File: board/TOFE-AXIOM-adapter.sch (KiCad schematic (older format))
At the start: 21 parts, among them CN1 C, U1 24AA01/24LC01B

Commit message: Adding annotations and parts.
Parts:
- CI2CN1, CI2CS1: footprint (none) -> Pin_Headers:Pin_Header_Straight_1x04
- CV1, CV2, CV3: footprint (none) -> SMD_Packages:SMD-1206_Pol
- CV4, CV5, CV6: footprint (none) -> Capacitors_SMD:C_1206_HandSoldering
- U2, U3: renamed from U?; footprint TO-220 -> Power_Integrations:TO-220
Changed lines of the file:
@@
 	5600 2850 5700 2850
 Wire Wire Line
-	5700 8300 5700 2850
+	5700 2850 5700 8300
 Wire Wire Line
 	5700 4150 5600 4150
@@
 Connection ~ 5700 7450
 Wire Wire Line
-	3800 8300 5700 8300
+	5700 8300 3800 8300
 Connection ~ 3800 7750
 Connection ~ 5700 7750
@@
 	10740 2390 10780 2390
 Wire Wire Line
-	10780 4720 10780 2390
+	10780 2390 10780 4720
 Wire Wire Line
 	10740 2690 10780 2690
@@
 Connection ~ 10780 3690
 Wire Wire Line
-	9010 4720 10780 4720
+	10780 4720 9010 4720
 Connection ~ 10780 4290
 Wire Wire Line
 	9040 4290 9010 4290
 Wire Wire Line
-	9010 3990 9010 4720
+	9010 4720 9010 3990
 Wire Wire Line
 	9010 3990 9040 3990
 Connection ~ 9010 4290
 $Comp
-L GND #PWR3
+L GND #PWR5
 U 1 1 56EBC288
 P 9940 4780
-F 0 "#PWR3" H 9940 4530 50  0001 C CNN
+F 0 "#PWR5" H 9940 4530 50  0001 C CNN
 F 1 "GND" H 9940 4630 50  0000 C CNN
 F 2 "" H 9940 4780 50  0000 C CNN
@@
 Connection ~ 10980 3390
 $Comp
-L GND #PWR5
+L GND #PWR7
 U 1 1 56EBCC2F
 P 11440 3500
-F 0 "#PWR5" H 11440 3250 50  0001 C CNN
+F 0 "#PWR7" H 11440 3250 50  0001 C CNN
 F 1 "GND" H 11440 3350 50  0000 C CNN
 F 2 "" H 11440 3500 50  0000 C CNN
@@
 	10740 5510 10780 5510
 Wire Wire Line
-	10780 7840 10780 5510
+	10780 5510 10780 7840
 Wire Wire Line
 	10740 5810 10780 5810
@@
 Connection ~ 10780 6810
 Wire Wire Line
-	9010 7840 10780 7840
+	10780 7840 9010 7840
 Connection ~ 10780 7410
 Wire Wire Line
 	9040 7410 9010 7410
 Wire Wire Line
-	9010 7110 9010 7840
+	9010 7840 9010 7110
 Wire Wire Line
 	9010 7110 9040 7110
 Connection ~ 9010 7410
 $Comp
-L GND #PWR4
+L GND #PWR6
 U 1 1 56EBD984
 P 9940 7900
-F 0 "#PWR4" H 9940 7650 50  0001 C CNN
+F 0 "#PWR6" H 9940 7650 50  0001 C CNN
 F 1 "GND" H 9940 7750 50  0000 C CNN
 F 2 "" H 9940 7900 50  0000 C CNN
@@
 Connection ~ 10980 6510
 $Comp
-L GND #PWR6
+L GND #PWR8
 U 1 1 56EBD9A0
 P 11440 6620
-F 0 "#PWR6" H 11440 6370 50  0001 C CNN
+F 0 "#PWR8" H 11440 6370 50  0001 C CNN
 F 1 "GND" H 11440 6470 50  0000 C CNN
 F 2 "" H 11440 6620 50  0000 C CNN
@@
 F 0 "CI2CS1" H 8290 5810 50  0000 C CNN
 F 1 "CONN_01X04" V 8390 5560 50  0000 C CNN
-F 2 "" H 8290 5560 50  0000 C CNN
+F 2 "Pin_Headers:Pin_Header_Straight_1x04" H 8290 5560 50  0001 C CNN
 F 3 "" H 8290 5560 50  0000 C CNN
 	1    8290 5560
@@
 F 0 "CI2CN1" H 8290 2690 50  0000 C CNN
 F 1 "CONN_01X04" V 8390 2440 50  0000 C CNN
-F 2 "" H 8290 2440 50  0000 C CNN
+F 2 "Pin_Headers:Pin_Header_Straight_1x04" H 8290 2440 50  0001 C CNN
 F 3 "" H 8290 2440 50  0000 C CNN
 	1    8290 2440
@@
 $EndComp
 $Comp
-L GND #PWR?
+L GND #PWR3
 U 1 1 56EF4A15
 P 8760 2290
-F 0 "#PWR?" H 8760 2040 50  0001 C CNN
+F 0 "#PWR3" H 8760 2040 50  0001 C CNN
 F 1 "GND" H 8760 2140 50  0000 C CNN
 F 2 "" H 8760 2290 50  0000 C CNN
@@
 	8760 2290 8490 2290
 $Comp
-L GND #PWR?
+L GND #PWR4
 U 1 1 56EF4B73
 P 8760 5410
-F 0 "#PWR?" H 8760 5160 50  0001 C CNN
+F 0 "#PWR4" H 8760 5160 50  0001 C CNN
 F 1 "GND" H 8760 5260 50  0000 C CNN
 F 2 "" H 8760 5410 50  0000 C CNN
@@
 	12170 1540 15770 1540
 $Comp
-L LM317T U?
+L LM317T U2
 U 1 1 56F236A7
 P 13010 2450
-F 0 "U?" H 12810 2650 50  0000 C CNN
+F 0 "U2" H 12810 2650 50  0000 C CNN
 F 1 "LM317T" H 13010 2650 50  0000 L CNN
-F 2 "TO-220" H 13010 2550 50  0000 C CIN
+F 2 "Power_Integrations:TO-220" H 13010 2550 50  0000 C CIN
 F 3 "" H 13010 2450 50  0000 C CNN
 	1    13010 2450
@@
 $EndComp
 $Comp
-L LM7805CT U?
+L LM7805CT U3
 U 1 1 56F237BB
 P 15010 2450
-F 0 "U?" H 14810 2650 50  0000 C CNN
+F 0 "U3" H 14810 2650 50  0000 C CNN
 F 1 "LM7805CT" H 15010 2650 50  0000 L CNN
-F 2 "TO-220" H 15010 2550 50  0000 C CIN
+F 2 "Power_Integrations:TO-220" H 15010 2550 50  0000 C CIN
 F 3 "" H 15010 2450 50  0000 C CNN
 	1    15010 2450
@@
 	12170 1740 15770 1740
 $Comp
-L GND #PWR?
+L GND #PWR11
 U 1 1 56F23FEE
 P 15010 2740
-F 0 "#PWR?" H 15010 2490 50  0001 C CNN
+F 0 "#PWR11" H 15010 2490 50  0001 C CNN
 F 1 "GND" H 15010 2590 50  0000 C CNN
 F 2 "" H 15010 2740 50  0000 C CNN
@@
 $EndComp
 $Comp
-L GND #PWR?
+L GND #PWR9
 U 1 1 56F2402D
 P 13010 2740
-F 0 "#PWR?" H 13010 2490 50  0001 C CNN
+F 0 "#PWR9" H 13010 2490 50  0001 C CNN
 F 1 "GND" H 13010 2590 50  0000 C CNN
 F 2 "" H 13010 2740 50  0000 C CNN
@@
 	14110 3200 14560 3200
 $Comp
-L GND #PWR?
+L GND #PWR10
 U 1 1 56F25B7E
 P 13710 3630
-F 0 "#PWR?" H 13710 3380 50  0001 C CNN
+F 0 "#PWR10" H 13710 3380 50  0001 C CNN
 F 1 "GND" H 13710 3480 50  0000 C CNN
 F 2 "" H 13710 3630 50  0000 C CNN
@@
 F 0 "CV3" H 13485 3460 50  0000 L CNN
 F 1 "CP1" H 13485 3260 50  0000 L CNN
-F 2 "" H 13460 3360 50  0000 C CNN
+F 2 "SMD_Packages:SMD-1206_Pol" H 13460 3360 50  0001 C CNN
 F 3 "" H 13460 3360 50  0000 C CNN
 	1    13460 3360
@@
 F 0 "CV4" H 14135 3470 50  0000 L CNN
 F 1 "C" H 14135 3270 50  0000 L CNN
-F 2 "" H 14148 3220 50  0000 C CNN
+F 2 "Capacitors_SMD:C_1206_HandSoldering" H 14148 3220 50  0001 C CNN
 F 3 "" H 14110 3370 50  0000 C CNN
 	1    14110 3370
@@
 F 0 "CV5" H 14365 3470 50  0000 L CNN
 F 1 "C" H 14365 3270 50  0000 L CNN
-F 2 "" H 14378 3220 50  0000 C CNN
+F 2 "Capacitors_SMD:C_1206_HandSoldering" H 14378 3220 50  0001 C CNN
 F 3 "" H 14340 3370 50  0000 C CNN
 	1    14340 3370
@@
 F 0 "CV6" H 14585 3470 50  0000 L CNN
 F 1 "C" H 14585 3270 50  0000 L CNN
-F 2 "" H 14598 3220 50  0000 C CNN
+F 2 "Capacitors_SMD:C_1206_HandSoldering" H 14598 3220 50  0001 C CNN
 F 3 "" H 14560 3370 50  0000 C CNN
 	1    14560 3370
@@
 F 0 "CV2" H 13255 3460 50  0000 L CNN
 F 1 "CP1" H 13255 3260 50  0000 L CNN
-F 2 "" H 13230 3360 50  0000 C CNN
+F 2 "SMD_Packages:SMD-1206_Pol" H 13230 3360 50  0001 C CNN
 F 3 "" H 13230 3360 50  0000 C CNN
 	1    13230 3360
@@
 F 0 "CV1" H 13025 3460 50  0000 L CNN
 F 1 "CP1" H 13025 3260 50  0000 L CNN
-F 2 "" H 13000 3360 50  0000 C CNN
+F 2 "SMD_Packages:SMD-1206_Pol" H 13000 3360 50  0001 C CNN
 F 3 "" H 13000 3360 50  0000 C CNN
 	1    13000 3360

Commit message: Updates from Dejan Stevanovic.
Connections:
- net labels removed: SCL, SDA
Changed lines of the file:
@@
 LIBS:valves
 LIBS:TOFE-AXIOM-adapter-cache
-LIBS:TOFE
-LIBS:axiom
-LIBS:EEPROM
 EELAYER 25 0
 EELAYER END
@@
 Connection ~ 9010 4290
 $Comp
-L GND #PWR5
+L GND #PWR01
 U 1 1 56EBC288
 P 9940 4780
-F 0 "#PWR5" H 9940 4530 50  0001 C CNN
+F 0 "#PWR01" H 9940 4530 50  0001 C CNN
 F 1 "GND" H 9940 4630 50  0000 C CNN
 F 2 "" H 9940 4780 50  0000 C CNN
@@
 Connection ~ 10980 3390
 $Comp
-L GND #PWR7
+L GND #PWR02
 U 1 1 56EBCC2F
 P 11440 3500
-F 0 "#PWR7" H 11440 3250 50  0001 C CNN
+F 0 "#PWR02" H 11440 3250 50  0001 C CNN
 F 1 "GND" H 11440 3350 50  0000 C CNN
 F 2 "" H 11440 3500 50  0000 C CNN
@@
 	11440 3500 11340 3500
 $Comp
-L GND #PWR1
+L GND #PWR03
 U 1 1 56EBCF33
 P 4700 8350
-F 0 "#PWR1" H 4700 8100 50  0001 C CNN
+F 0 "#PWR03" H 4700 8100 50  0001 C CNN
 F 1 "GND" H 4700 8200 50  0000 C CNN
 F 2 "" H 4700 8350 50  0000 C CNN
@@
 GND
 Text Label 4200 9300 0    60   ~ 12
-SCL
+S_SCL
 Text Label 4200 9700 0    60   ~ 12
-SDA
+S_SDA
 Text Notes 5050 9000 0    60   ~ 12
 EEPROM
@@
 	6000 10050 6000 10100
 $Comp
-L GND #PWR2
+L GND #PWR04
 U 1 1 56EBC6DB
 P 6000 9350
-F 0 "#PWR2" H 6000 9100 50  0001 C CNN
+F 0 "#PWR04" H 6000 9100 50  0001 C CNN
 F 1 "GND" H 6000 9200 50  0000 C CNN
 F 2 "" H 6000 9350 50  0000 C CNN
@@
 Connection ~ 9010 7410
 $Comp
-L GND #PWR6
+L GND #PWR05
 U 1 1 56EBD984
 P 9940 7900
-F 0 "#PWR6" H 9940 7650 50  0001 C CNN
+F 0 "#PWR05" H 9940 7650 50  0001 C CNN
 F 1 "GND" H 9940 7750 50  0000 C CNN
 F 2 "" H 9940 7900 50  0000 C CNN
@@
 Connection ~ 10980 6510
 $Comp
-L GND #PWR8
+L GND #PWR06
 U 1 1 56EBD9A0
 P 11440 6620
-F 0 "#PWR8" H 11440 6370 50  0001 C CNN
+F 0 "#PWR06" H 11440 6370 50  0001 C CNN
 F 1 "GND" H 11440 6470 50  0000 C CNN
 F 2 "" H 11440 6620 50  0000 C CNN
@@
 $EndComp
 $Comp
-L GND #PWR3
+L GND #PWR07
 U 1 1 56EF4A15
 P 8760 2290
-F 0 "#PWR3" H 8760 2040 50  0001 C CNN
+F 0 "#PWR07" H 8760 2040 50  0001 C CNN
 F 1 "GND" H 8760 2140 50  0000 C CNN
 F 2 "" H 8760 2290 50  0000 C CNN
@@
 	8760 2290 8490 2290
 $Comp
-L GND #PWR4
+L GND #PWR08
 U 1 1 56EF4B73
 P 8760 5410
-F 0 "#PWR4" H 8760 5160 50  0001 C CNN
+F 0 "#PWR08" H 8760 5160 50  0001 C CNN
 F 1 "GND" H 8760 5260 50  0000 C CNN
 F 2 "" H 8760 5410 50  0000 C CNN
@@
 	12170 1740 15770 1740
 $Comp
-L GND #PWR11
+L GND #PWR09
 U 1 1 56F23FEE
 P 15010 2740
-F 0 "#PWR11" H 15010 2490 50  0001 C CNN
+F 0 "#PWR09" H 15010 2490 50  0001 C CNN
 F 1 "GND" H 15010 2590 50  0000 C CNN
 F 2 "" H 15010 2740 50  0000 C CNN
@@
 $EndComp
 $Comp
-L GND #PWR9
+L GND #PWR010
 U 1 1 56F2402D
 P 13010 2740
-F 0 "#PWR9" H 13010 2490 50  0001 C CNN
+F 0 "#PWR010" H 13010 2490 50  0001 C CNN
 F 1 "GND" H 13010 2590 50  0000 C CNN
 F 2 "" H 13010 2740 50  0000 C CNN
@@
 	14110 3200 14560 3200
 $Comp
-L GND #PWR10
+L GND #PWR011
 U 1 1 56F25B7E
 P 13710 3630
-F 0 "#PWR10" H 13710 3380 50  0001 C CNN
+F 0 "#PWR011" H 13710 3380 50  0001 C CNN
 F 1 "GND" H 13710 3480 50  0000 C CNN
 F 2 "" H 13710 3630 50  0000 C CNN

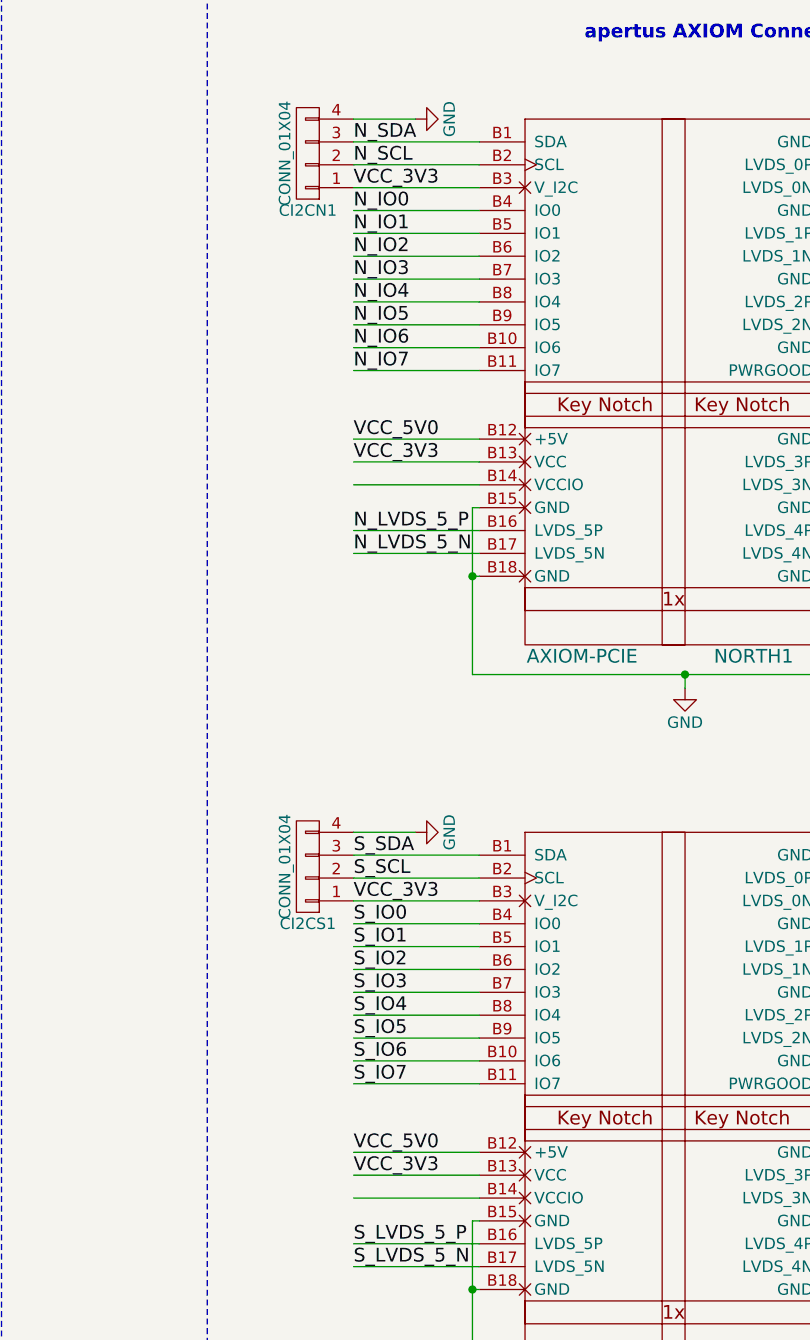
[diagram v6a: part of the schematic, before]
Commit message: Make VCC names consistent.
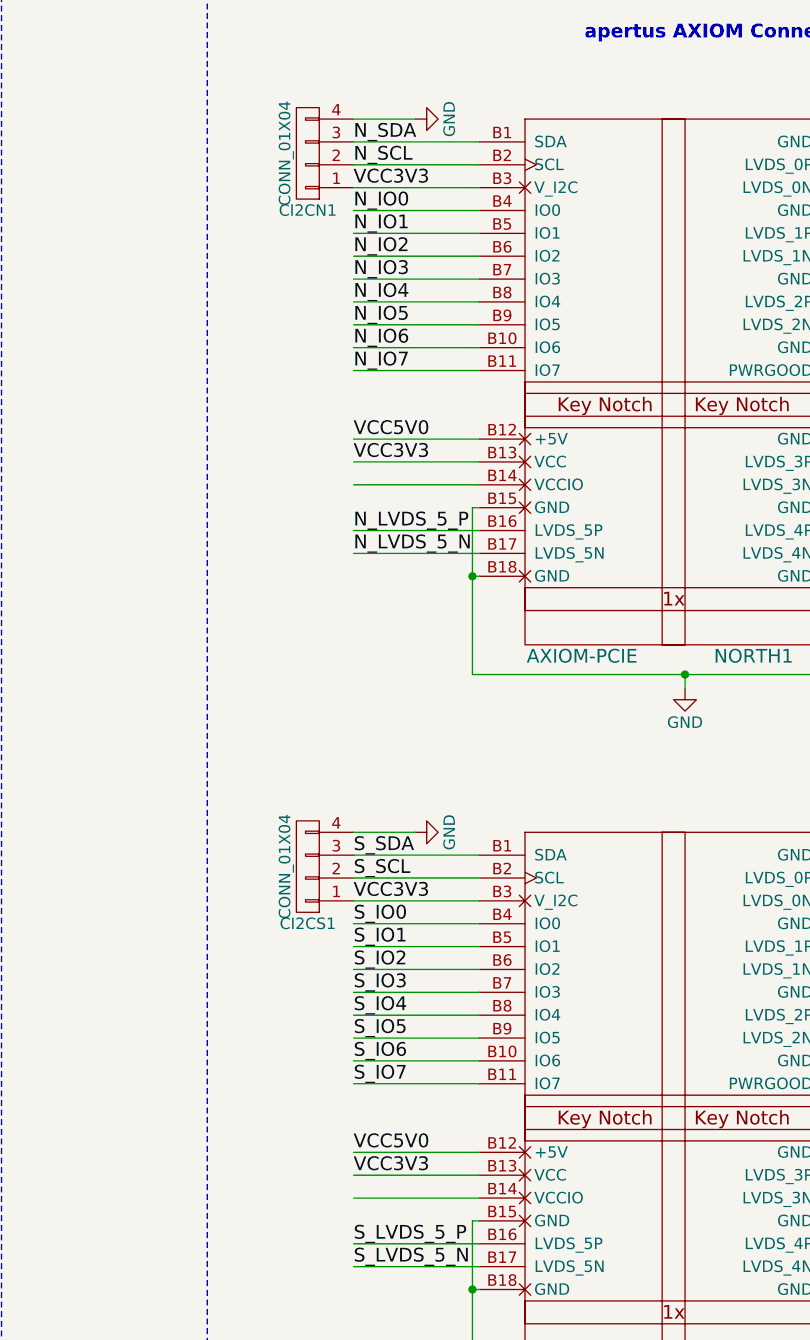
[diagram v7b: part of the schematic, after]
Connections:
- net labels added: VCC5V0
- net labels removed: VCC_3V3, VCC_5V0
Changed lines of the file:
@@
 	8490 3690 9040 3690
 Text Label 8490 3690 0    60   ~ 0
-VCC_5V0
+VCC5V0
 Text Label 8490 2590 0    60   ~ 0
-VCC_3V3
+VCC3V3
 Wire Wire Line
 	10740 3390 10980 3390
@@
 	8490 6810 9040 6810
 Text Label 8490 6810 0    60   ~ 0
-VCC_5V0
+VCC5V0
 Text Label 8490 5710 0    60   ~ 0
-VCC_3V3
+VCC3V3
 Wire Wire Line
 	10740 6510 10980 6510
@@
 	11440 6620 11340 6620
 Text Label 8490 3790 0    60   ~ 0
-VCC_3V3
+VCC3V3
 Text Label 8490 6910 0    60   ~ 0
-VCC_3V3
+VCC3V3
 $Comp
 L CONN_01X04 CI2CS1

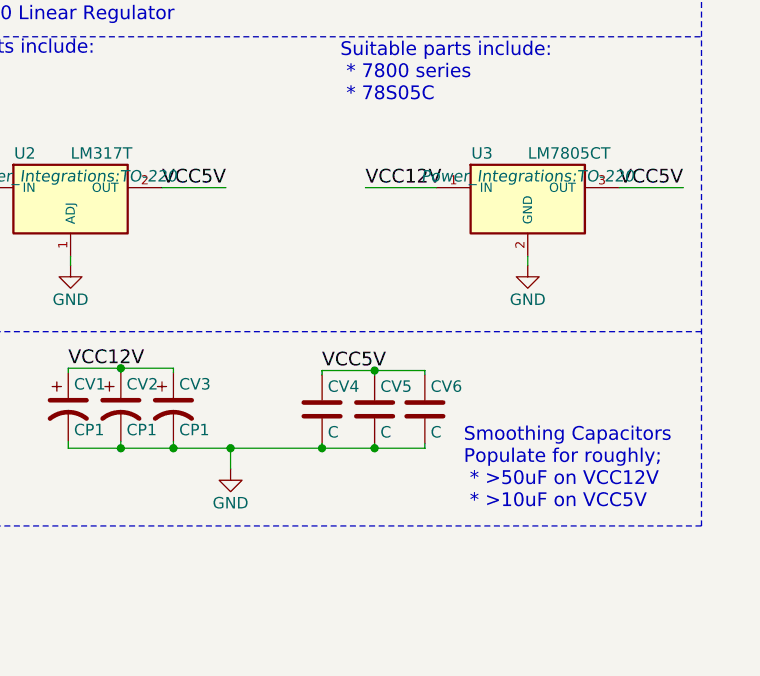
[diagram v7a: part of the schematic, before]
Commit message: More fixing power supply.
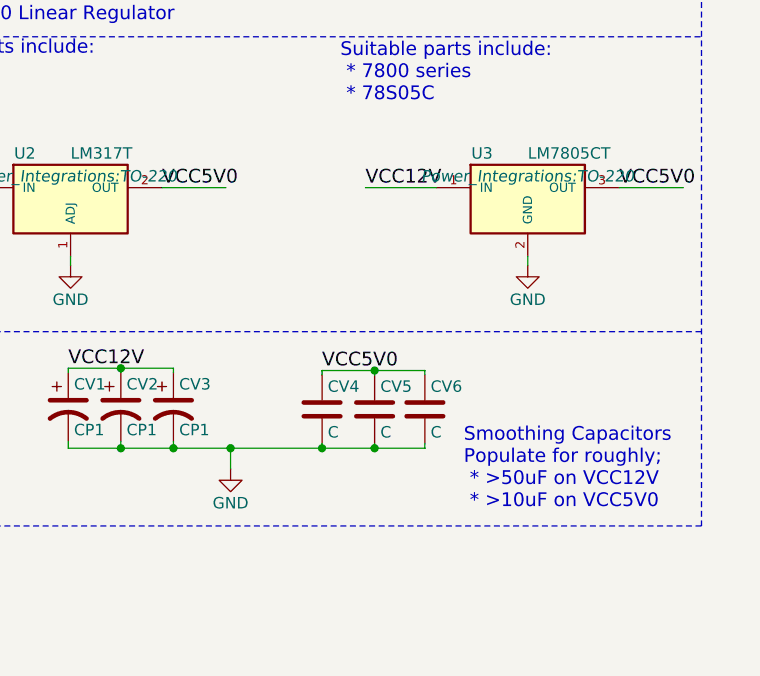
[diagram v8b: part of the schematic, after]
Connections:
- net labels removed: VCC5V
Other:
- note added: "Smoothing Capacitors\nPopulate for roughly;\n * >50uF on VCC12V\n * >10uF on VCC5V0\n"
- note removed: "Smoothing Capacitors\nPopulate for roughly;\n * >50uF on VCC12V\n * >10uF on VCC5V\n"
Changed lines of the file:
@@
 	12610 2400 12300 2400
 Text Label 13410 2400 0    60   ~ 0
-VCC5V
+VCC5V0
 Wire Wire Line
 	13410 2400 13690 2400
 Text Label 15410 2400 0    60   ~ 0
-VCC5V
+VCC5V0
 Wire Wire Line
 	15410 2400 15690 2400
@@
 VCC12V
 Text Label 14110 3200 0    60   ~ 0
-VCC5V
+VCC5V0
 Wire Wire Line
 	13000 3190 13460 3190
@@
 	15770 3030 12170 3030
 Text Notes 14730 3810 0    60   ~ 0
-Smoothing Capacitors\nPopulate for roughly;\n * >50uF on VCC12V\n * >10uF on VCC5V\n
+Smoothing Capacitors\nPopulate for roughly;\n * >50uF on VCC12V\n * >10uF on VCC5V0\n
 $EndSCHEMATC
